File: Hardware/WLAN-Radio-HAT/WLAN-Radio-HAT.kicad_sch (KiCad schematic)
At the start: 35 parts, among them J1 Pi, J2 Amp, J3 LCD, J4 Next, J5 Prev, J6 Supply, U1 PCM5100A, U2 AMP150

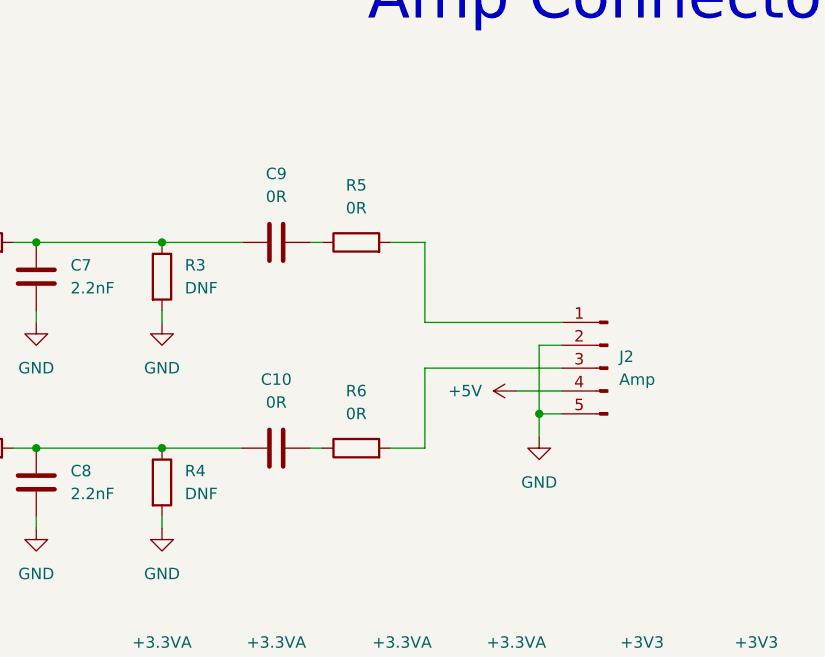
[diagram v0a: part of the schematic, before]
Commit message: removed unnecessary filter components
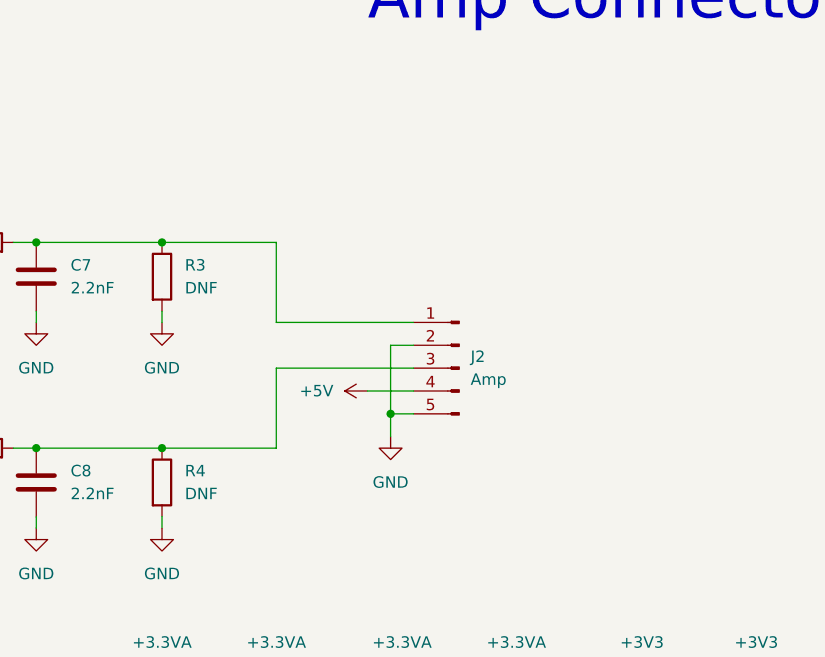
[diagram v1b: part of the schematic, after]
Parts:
- removed C10, C9: 0R, Capacitor_SMD:C_0805_2012Metric, symbol Device:C
- removed R5, R6: 0R, Resistor_SMD:R_0805_2012Metric, symbol Device:R
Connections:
- net at C8.1, R2.2, R4.1: now also J2.3 (Pin_3)
- net at C7.1, R1.2, R3.1: now also J2.1 (Pin_1)
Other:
- moved on the sheet: J2

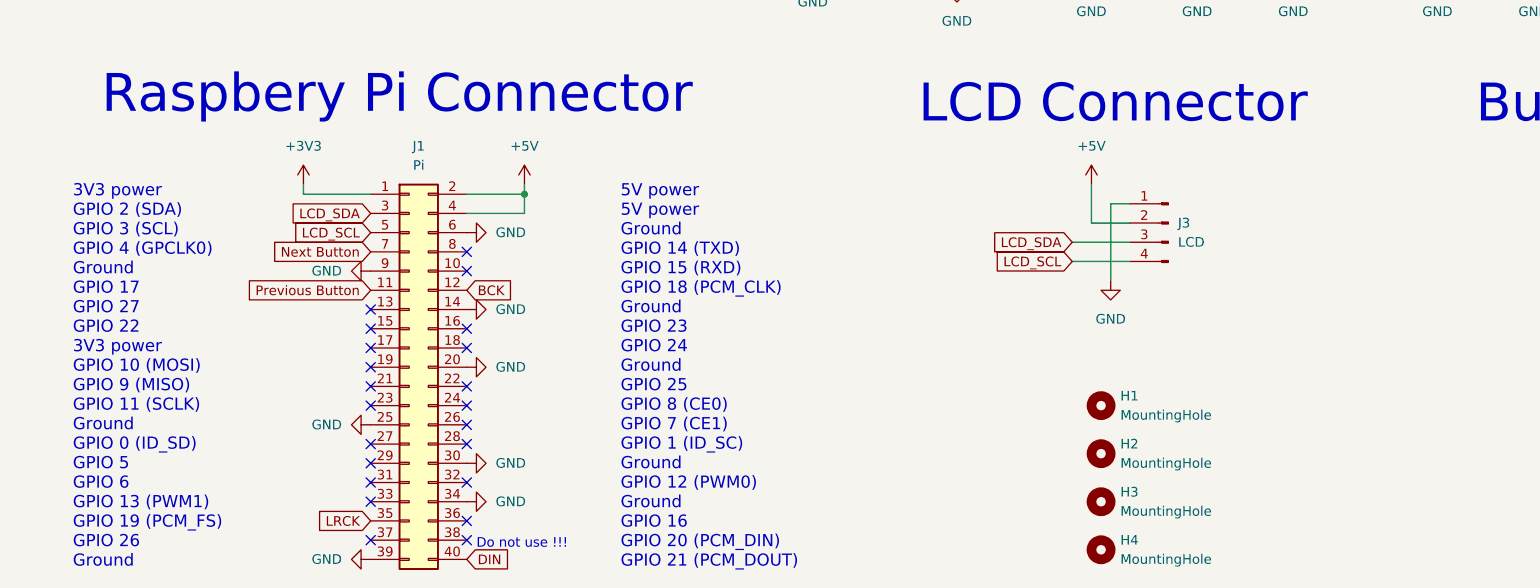
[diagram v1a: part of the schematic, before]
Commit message: add alternate LCD connector and use better 3v3 supply pin
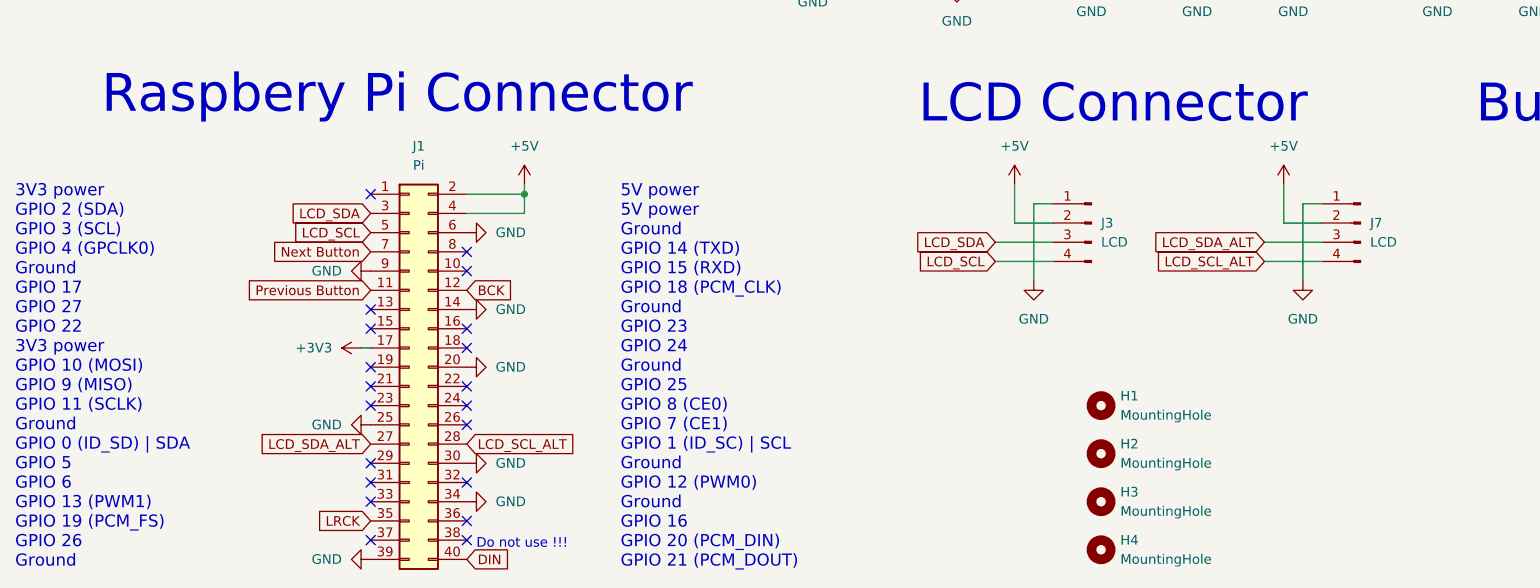
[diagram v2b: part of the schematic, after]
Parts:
- added J7: LCD, Connector_PinHeader_2.54mm:PinHeader_1x04_P2.54mm_Vertical, symbol Connector:Conn_01x04_Pin
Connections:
- net +3V3: now also J1.17 (Pin_17); no longer J1.1 (Pin_1)
- net +5V: now also J7.2 (Pin_2)
- net GND: now also J7.1 (Pin_1)
- net LCD_SDA_ALT: now reaches J1.27 (Pin_27)
- net LCD_SDA_ALT: now also J7.3 (Pin_3)
- net LCD_SCL_ALT: now reaches J1.28 (Pin_28)
- net LCD_SCL_ALT: now also J7.4 (Pin_4)
- no-connect marks 22 -> 20
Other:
- note added: "3V3 power GPIO 2 (SDA) GPIO 3 (SCL) GPIO 4 (GPCLK0) Ground GPIO 17 GPIO 27 GPIO 22 3V3 power GPIO 10 (MOSI) GPIO 9 (MISO) GPIO 11 (SCLK) Ground GPIO 0 (ID_SD) | SDA GPIO 5 GPIO 6 GPIO 13 (PWM1) GPIO 19 (PCM_FS) GPIO 26 Ground"
- note added: "5V power 5V power Ground GPIO 14 (TXD) GPIO 15 (RXD) GPIO 18 (PCM_CLK) Ground GPIO 23 GPIO 24 Ground GPIO 25 GPIO 8 (CE0) GPIO 7 (CE1) GPIO 1 (ID_SC) | SCL Ground GPIO 12 (PWM0) Ground GPIO 16 GPIO 20 (PCM_DIN) GPIO 21 (PCM_DOUT)"
- note removed: "3V3 power GPIO 2 (SDA) GPIO 3 (SCL) GPIO 4 (GPCLK0) Ground GPIO 17 GPIO 27 GPIO 22 3V3 power GPIO 10 (MOSI) GPIO 9 (MISO) GPIO 11 (SCLK) Ground GPIO 0 (ID_SD) GPIO 5 GPIO 6 GPIO 13 (PWM1) GPIO 19 (PCM_FS) GPIO 26 Ground"
- note removed: "5V power 5V power Ground GPIO 14 (TXD) GPIO 15 (RXD) GPIO 18 (PCM_CLK) Ground GPIO 23 GPIO 24 Ground GPIO 25 GPIO 8 (CE0) GPIO 7 (CE1) GPIO 1 (ID_SC) Ground GPIO 12 (PWM0) Ground GPIO 16 GPIO 20 (PCM_DIN) GPIO 21 (PCM_DOUT)"
- moved on the sheet: J3
